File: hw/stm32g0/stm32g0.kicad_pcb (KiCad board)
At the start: 4 copper layers, 80 x 40 mm, 74 parts, among them J101 Barrel_Jack_Switch, J102 Screw_Terminal_01x03, J201 Conn_01x06, J202 Conn_01x04, J203 Conn_01x05, Q101 BC817, SW401 SW_Push, SW402 SW_Push, SW403 SW_Push, SW404 SW_Push, SW405 SW_Push, SW406 SW_Push, U201 STM32G030K8Tx, U202 74AHCT125, U203 CAT24C256, U301 VS1838B, U401 4050, U501 AMS1117-3.3

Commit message: chore(hw): improve layout
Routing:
- net GND: track 144.7 -> 155.6 mm, vias 51 -> 50
- net +5V: track 145.7 -> 141.7 mm
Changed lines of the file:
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@@
 	)
 	(segment
-		(start 192.151 89.615)
+		(start 184.277 90.424)
+		(end 191.897 90.424)
+		(width 1.5)
+		(layer "In2.Cu")
+		(net 1)
+	)
+	(segment
+		(start 192.706 89.615)
 		(end 194.183 89.615)
 		(width 1.5)
-		(layer "In1.Cu")
+		(layer "In2.Cu")
 		(net 1)
 	)
 	(segment
 		(start 182.118 91.069)
-		(end 182.763 90.424)
+		(end 183.632 91.069)
 		(width 1.5)
-		(layer "In1.Cu")
-		(net 1)
-	)
-	(segment
-		(start 191.342 90.424)
-		(end 192.151 89.615)
+		(layer "In2.Cu")
+		(net 1)
+	)
+	(segment
+		(start 191.897 90.424)
+		(end 192.706 89.615)
 		(width 1.5)
-		(layer "In1.Cu")
-		(net 1)
-	)
-	(segment
-		(start 182.763 90.424)
-		(end 191.342 90.424)
+		(layer "In2.Cu")
+		(net 1)
+	)
+	(segment
+		(start 183.632 91.069)
+		(end 184.277 90.424)
 		(width 1.5)
-		(layer "In1.Cu")
+		(layer "In2.Cu")
+		(net 1)
+	)
+	(segment
+		(start 171.577 95.123)
+		(end 175.26 98.806)
+		(width 0.5)
+		(layer "B.Cu")
 		(net 1)
 	)
@@
 	)
 	(segment
-		(start 182.118 92.869)
-		(end 173.069 92.869)
-		(width 0.5)
-		(layer "B.Cu")
-		(net 1)
-	)
-	(segment
 		(start 142.113 111.379)
 		(end 140.716 111.379)
@@
 	)
 	(segment
+		(start 175.26 98.806)
+		(end 175.26 100.33)
+		(width 0.5)
+		(layer "B.Cu")
+		(net 1)
+	)
+	(segment
 		(start 162.052 102.23501)
 		(end 169.672 102.23501)
@@
 		(end 161.544 109.728)
 		(width 0.3)
-		(layer "B.Cu")
-		(net 1)
-	)
-	(segment
-		(start 175.26 100.33)
-		(end 175.26 98.425)
-		(width 0.5)
 		(layer "B.Cu")
 		(net 1)
@@
 	)
 	(segment
-		(start 180.499 94.488)
-		(end 182.118 92.869)
-		(width 0.5)
-		(layer "B.Cu")
-		(net 1)
-	)
-	(segment
-		(start 175.26 98.425)
-		(end 179.197 94.488)
-		(width 0.5)
-		(layer "B.Cu")
-		(net 1)
-	)
-	(segment
 		(start 175.26 100.33)
 		(end 175.26 104.77499)
@@
 	)
 	(segment
+		(start 173.831 92.869)
+		(end 171.577 95.123)
+		(width 0.7)
+		(layer "B.Cu")
+		(net 1)
+	)
+	(segment
 		(start 171.57701 100.33)
 		(end 175.26 100.33)
@@
 	)
 	(segment
+		(start 182.118 92.869)
+		(end 173.831 92.869)
+		(width 0.7)
+		(layer "B.Cu")
+		(net 1)
+	)
+	(segment
 		(start 156.464 100.457)
 		(end 160.27399 100.457)
@@
 	)
 	(segment
-		(start 173.069 92.869)
-		(end 171.577 94.361)
-		(width 0.5)
-		(layer "B.Cu")
-		(net 1)
-	)
-	(segment
-		(start 179.197 94.488)
-		(end 180.499 94.488)
-		(width 0.5)
-		(layer "B.Cu")
-		(net 1)
-	)
-	(segment
 		(start 143.764 109.728)
 		(end 142.113 111.379)
@@
 		(layer "F.Cu")
 		(net 2)
+	)
+	(segment
+		(start 185.674 103.886)
+		(end 185.674 105.283)
+		(width 0.3)
+		(layer "F.Cu")
+		(net 3)
 	)
 	(segment
@@
 	)
 	(segment
-		(start 185.547 103.759)
-		(end 185.674 103.886)
-		(width 0.3)
-		(layer "F.Cu")
-		(net 3)
-	)
-	(segment
 		(start 153.035 101.854)
 		(end 152.908 101.727)
@@
 		(end 160.4225 90.0645)
 		(width 0.4)
-		(layer "F.Cu")
-		(net 3)
-	)
-	(segment
-		(start 185.674 103.886)
-		(end 185.674 106.172)
-		(width 0.3)
 		(layer "F.Cu")
 		(net 3)
@@
 	)
 	(segment
+		(start 185.547 103.759)
+		(end 185.674 103.886)
+		(width 0.3)
+		(layer "F.Cu")
+		(net 3)
+	)
+	(segment
 		(start 179.4256 79.0956)
 		(end 179.832 79.502)
@@
 	)
 	(segment
+		(start 185.674 105.283)
+		(end 185.547 105.41)
+		(width 0.3)
+		(layer "F.Cu")
+		(net 3)
+	)
+	(segment
 		(start 181.864 78.486)
 		(end 182.118 78.232)
@@
 	)
 	(via
-		(at 176.784 94.361)
-		(size 0.8)
-		(drill 0.4)
-		(layers "F.Cu" "B.Cu")
-		(free yes)
-		(net 3)
-	)
-	(via
 		(at 190.119 104.14)
 		(size 0.8)
@@
 		(layers "F.Cu" "B.Cu")
 		(free yes)
+		(net 3)
+	)
+	(segment
+		(start 188.976 104.14)
+		(end 190.119 104.14)
+		(width 0.3)
+		(layer "B.Cu")
+		(net 3)
+	)
+	(segment
+		(start 155.406 96.944337)
+		(end 155.406 90.974)
+		(width 0.3)
+		(layer "B.Cu")
+		(net 3)
+	)
+	(segment
+		(start 147.447 104.648)
+		(end 147.702337 104.648)
+		(width 0.3)
+		(layer "B.Cu")
+		(net 3)
+	)
+	(segment
+		(start 160.528 82.804)
+		(end 165.227 82.804)
+		(width 0.3)
+		(layer "B.Cu")
+		(net 3)
+	)
+	(segment
+		(start 186.055 100.457)
+		(end 186.055 101.219)
+		(width 0.3)
+		(layer "B.Cu")
+		(net 3)
+	)
+	(segment
+		(start 159.766 83.058)
+		(end 160.274 83.058)
+		(width 0.3)
+		(layer "B.Cu")
+		(net 3)
+	)
+	(segment
+		(start 186.444 100.068)
+		(end 186.055 100.457)
+		(width 0.3)
+		(layer "B.Cu")
+		(net 3)
+	)
+	(segment
+		(start 186.055 101.219)
+		(end 188.976 104.14)
+		(width 0.3)
+		(layer "B.Cu")
+		(net 3)
+	)
+	(segment
+		(start 184.794214 81.907)
+		(end 186.444 83.556786)
+		(width 0.3)
+		(layer "B.Cu")
+		(net 3)
+	)
+	(segment
+		(start 160.274 83.058)
+		(end 160.528 82.804)
+		(width 0.3)
+		(layer "B.Cu")
 		(net 3)
 	)
@@
 	)
 	(segment
-		(start 155.406 96.944337)
-		(end 155.406 90.974)
-		(width 0.3)
-		(layer "B.Cu")
-		(net 3)
-	)
-	(segment
-		(start 184.794214 81.907)
-		(end 186.444 83.556786)
-		(width 0.3)
-		(layer "B.Cu")
-		(net 3)
-	)
-	(segment
-		(start 147.447 104.648)
-		(end 147.702337 104.648)
+		(start 147.702337 104.648)
+		(end 155.406 96.944337)
+		(width 0.3)
+		(layer "B.Cu")
+		(net 3)
+	)
+	(segment
+		(start 155.406 90.974)
+		(end 155.829 90.551)
 		(width 0.3)
 		(layer "B.Cu")
@@
 	)
 	(segment
+		(start 147.066 105.029)
+		(end 147.447 104.648)
+		(width 0.3)
+		(layer "B.Cu")
+		(net 3)
+	)
+	(segment
 		(start 165.227 82.804)
 		(end 166.124 81.907)
-		(width 0.3)
-		(layer "B.Cu")
-		(net 3)
-	)
-	(segment
-		(start 186.444 100.068)
-		(end 186.055 100.457)
-		(width 0.3)
-		(layer "B.Cu")
-		(net 3)
-	)
-	(segment
-		(start 147.702337 104.648)
-		(end 155.406 96.944337)
-		(width 0.3)
-		(layer "B.Cu")
-		(net 3)
-	)
-	(segment
-		(start 155.406 90.974)
-		(end 155.829 90.551)
-		(width 0.3)
-		(layer "B.Cu")
-		(net 3)
-	)
-	(segment
-		(start 147.066 105.029)
-		(end 147.447 104.648)
 		(width 0.3)
 		(layer "B.Cu")
@@
 	)
 	(segment
+		(start 175.895 86.487)
+		(end 161.163 86.487)
+		(width 0.3)
+		(layer "B.Cu")
+		(net 14)
+	)
+	(segment
+		(start 161.163 86.487)
+		(end 160.274 85.598)
+		(width 0.3)
+		(layer "B.Cu")
+		(net 14)
+	)
+	(segment
 		(start 150.741 84.701)
 		(end 149.606 83.566)
@@
 	)
 	(segment
-		(start 174.879 86.106)
-		(end 160.782 86.106)
-		(width 0.3)
-		(layer "B.Cu")
-		(net 14)
-	)
-	(segment
-		(start 160.782 86.106)
-		(end 160.274 85.598)
-		(width 0.3)
-		(layer "B.Cu")
-		(net 14)
-	)
-	(segment
-		(start 175.895 86.487)
-		(end 175.26 86.487)
-		(width 0.3)
-		(layer "B.Cu")
-		(net 14)
-	)
-	(segment
 		(start 148.463 83.566)
 		(end 147.193 82.296)
@@
 		(width 0.3)
 		(layer "B.Cu")
-		(net 14)
-	)
-	(segment
-		(start 175.26 86.487)
-		(end 174.879 86.106)
-		(width 0.3)
-		(layer "B.Cu")

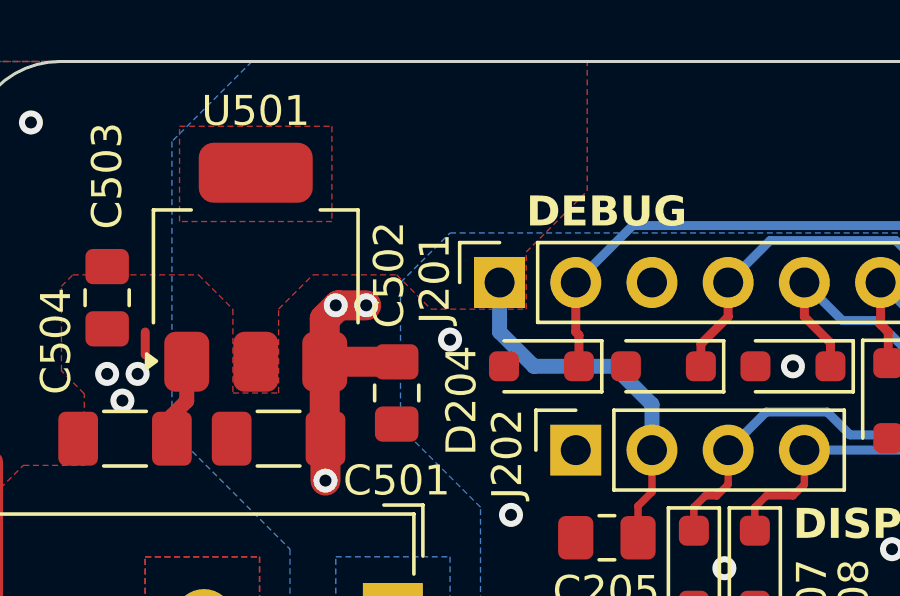
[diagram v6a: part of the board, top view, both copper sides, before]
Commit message: chore(hw): change debug port to pin header
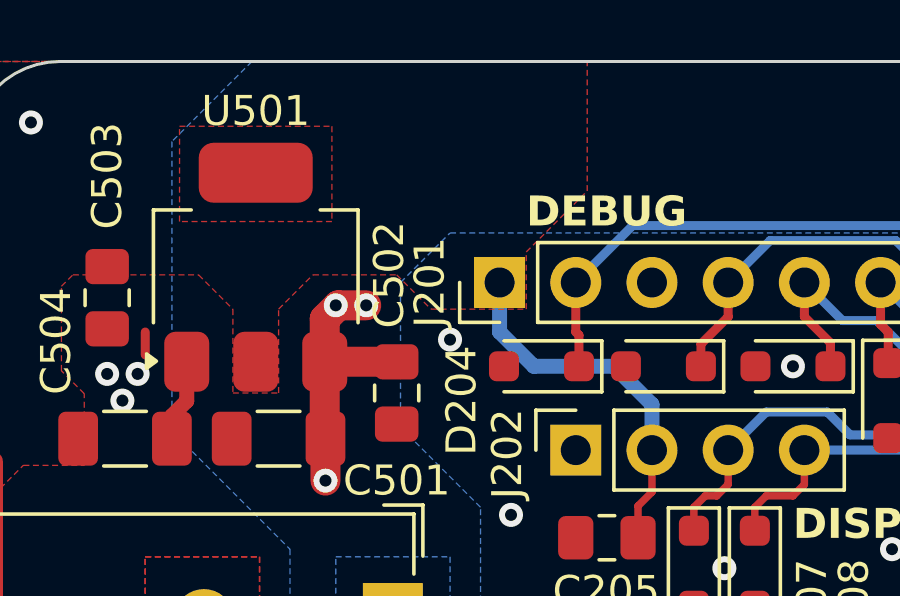
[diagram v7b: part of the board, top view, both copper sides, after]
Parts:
- J201: footprint Connector_PinSocket_2.54mm:PinSocket_1x06_P2.54mm_Vertical -> Connector_PinHeader_2.54mm:PinHeader_1x06_P2.54mm_Vertical
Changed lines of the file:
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@@
 		)
 	)
-	(footprint "Connector_PinSocket_2.54mm:PinSocket_1x06_P2.54mm_Vertical"
+	(footprint "Connector_PinHeader_2.54mm:PinHeader_1x06_P2.54mm_Vertical"
 		(layer "F.Cu")
 		(at 137.033 82.296 90)
-		(descr "Through hole straight socket strip, 1x06, 2.54mm pitch, single row (from Kicad 4.0.7), script generated")
-		(tags "Through hole socket strip THT 1x06 2.54mm single row")
+		(descr "Through hole straight pin header, 1x06, 2.54mm pitch, single row")
+		(tags "Through hole pin header THT 1x06 2.54mm single row")
 		(property "Reference" "J201"
-			(at 0.127 -2.159 -90)
+			(at 0 -2.33 90)
 			(layer "F.SilkS")
 			(effects
@@
 		)
 		(property "Value" "Conn_01x06"
-			(at 2.54 -2.159 -90)
+			(at 0 15.03 90)
 			(layer "F.Fab")
 			(effects
@@
 			)
 		)
-		(property "Footprint" "Connector_PinSocket_2.54mm:PinSocket_1x06_P2.54mm_Vertical"
+		(property "Footprint" "Connector_PinHeader_2.54mm:PinHeader_1x06_P2.54mm_Vertical"
 			(at 0 0 90)
 			(unlocked yes)
@@
 		(attr through_hole dnp)
 		(fp_line
-			(start 1.33 -1.33)
-			(end 1.33 0)
-			(stroke
-				(width 0.12)
-				(type solid)
-			)
-			(layer "F.SilkS")
-		)
-		(fp_line
-			(start 0 -1.33)
-			(end 1.33 -1.33)
+			(start -1.33 -1.33)
+			(end 0 -1.33)
+			(stroke
+				(width 0.12)
+				(type solid)
+			)
+			(layer "F.SilkS")
+		)
+		(fp_line
+			(start -1.33 0)
+			(end -1.33 -1.33)
 			(stroke
 				(width 0.12)
@@
 		)
 		(fp_line
-			(start 1.75 -1.8)
-			(end 1.75 14.45)
+			(start 1.8 -1.8)
+			(end -1.8 -1.8)
 			(stroke
 				(width 0.05)
@@
 		(fp_line
 			(start -1.8 -1.8)
-			(end 1.75 -1.8)
-			(stroke
-				(width 0.05)
-				(type solid)
-			)
-			(layer "F.CrtYd")
-		)
-		(fp_line
-			(start 1.75 14.45)
-			(end -1.8 14.45)
-			(stroke
-				(width 0.05)
-				(type solid)
-			)
-			(layer "F.CrtYd")
-		)
-		(fp_line
-			(start -1.8 14.45)
-			(end -1.8 -1.8)
-			(stroke
-				(width 0.05)
-				(type solid)
-			)
-			(layer "F.CrtYd")
-		)
-		(fp_line
-			(start 0.635 -1.27)
-			(end 1.27 -0.635)
-			(stroke
-				(width 0.1)
-				(type solid)
-			)
-			(layer "F.Fab")
-		)
-		(fp_line
-			(start -1.27 -1.27)
-			(end 0.635 -1.27)
-			(stroke
-				(width 0.1)
-				(type solid)
-			)
-			(layer "F.Fab")
-		)
-		(fp_line
-			(start 1.27 -0.635)
+			(end -1.8 14.5)
+			(stroke
+				(width 0.05)
+				(type solid)
+			)
+			(layer "F.CrtYd")
+		)
+		(fp_line
+			(start 1.8 14.5)
+			(end 1.8 -1.8)
+			(stroke
+				(width 0.05)
+				(type solid)
+			)
+			(layer "F.CrtYd")
+		)
+		(fp_line
+			(start -1.8 14.5)
+			(end 1.8 14.5)
+			(stroke
+				(width 0.05)
+				(type solid)
+			)
+			(layer "F.CrtYd")
+		)
+		(fp_line
+			(start 1.27 -1.27)
 			(end 1.27 13.97)
+			(stroke
+				(width 0.1)
+				(type solid)
+			)
+			(layer "F.Fab")
+		)
+		(fp_line
+			(start -0.635 -1.27)
+			(end 1.27 -1.27)
+			(stroke
+				(width 0.1)
+				(type solid)
+			)
+			(layer "F.Fab")
+		)
+		(fp_line
+			(start -1.27 -0.635)
+			(end -0.635 -1.27)
 			(stroke
 				(width 0.1)
@@
 		(fp_line
 			(start -1.27 13.97)
-			(end -1.27 -1.27)
+			(end -1.27 -0.635)
 			(stroke
 				(width 0.1)
@@
 		)
 		(fp_text user "${REFERENCE}"
-			(at 0 6.35 0)
+			(at 0 6.35 180)
 			(layer "F.Fab")
 			(effects
@@
 			(pintype "passive")
 		)
-		(model "${KICAD8_3DMODEL_DIR}/Connector_PinSocket_2.54mm.3dshapes/PinSocket_1x06_P2.54mm_Vertical.wrl"
+		(model "${KICAD8_3DMODEL_DIR}/Connector_PinHeader_2.54mm.3dshapes/PinHeader_1x06_P2.54mm_Vertical.wrl"
 			(offset
 				(xyz 0 0 0)

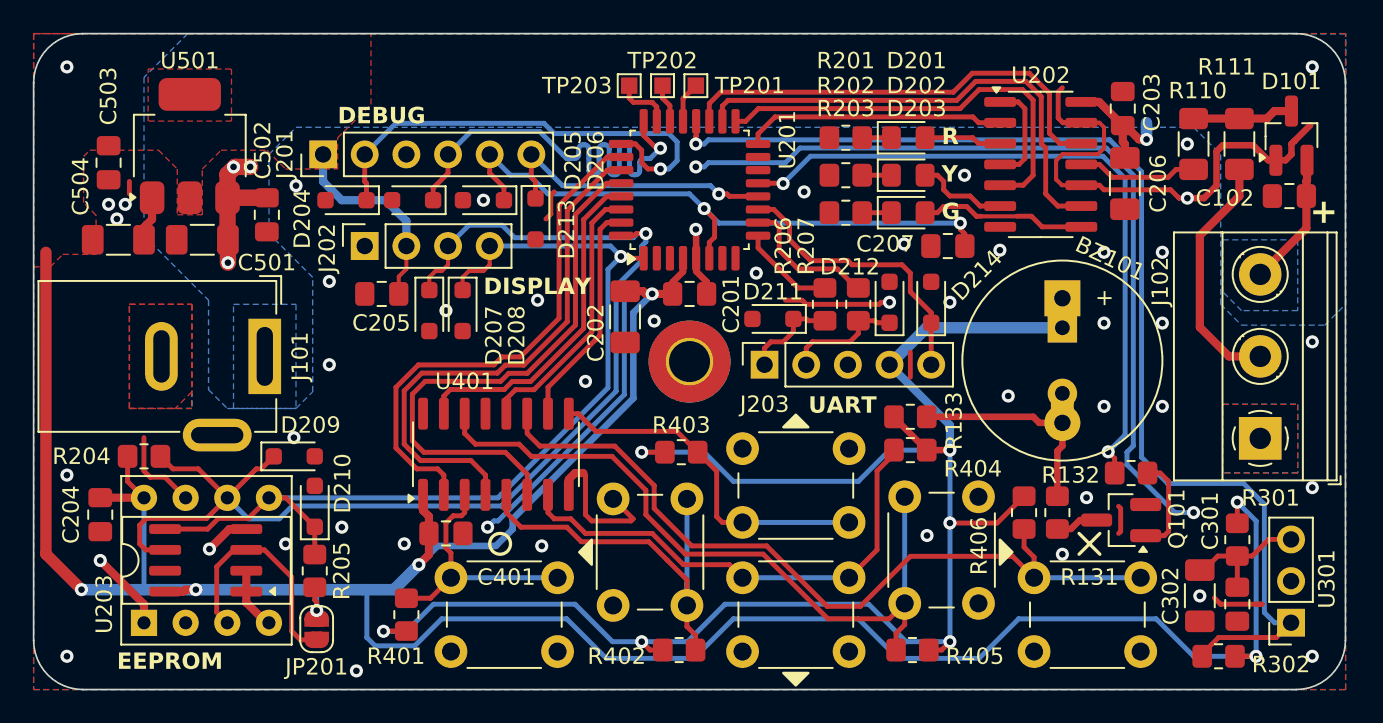
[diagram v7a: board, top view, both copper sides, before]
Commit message: chore(hw): improve i2c layout
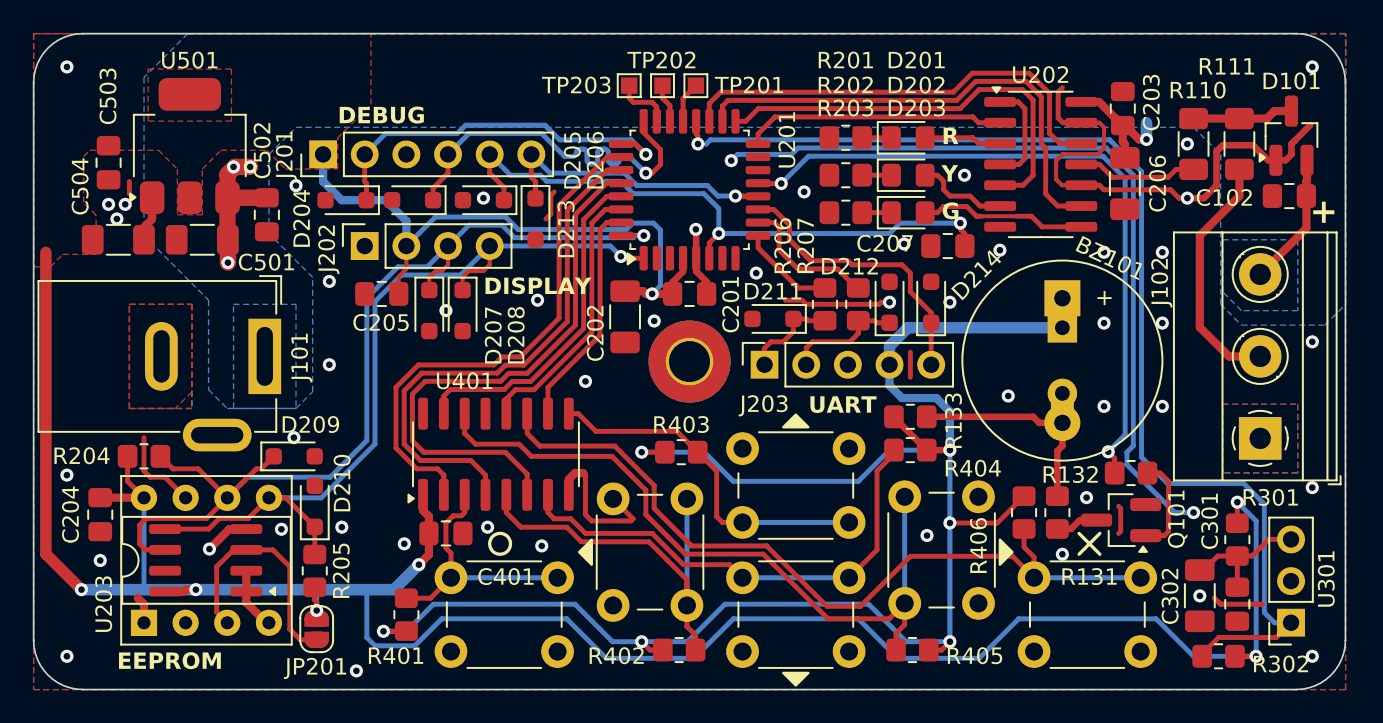
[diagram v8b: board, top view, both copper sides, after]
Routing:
- net GND: track 155.6 -> 131.8 mm
- net /CPU/I2C_SCL: track 73.7 -> 60.4 mm
- net /CPU/I2C_SDA: track 58.5 -> 51.6 mm
- net /CPU/SWCLK: track 29.0 -> 23.2 mm
- net /CPU/SWDIO: track 29.2 -> 23.5 mm
- net +3.3V: track 181.1 -> 177.6 mm
- net +5V: track 141.7 -> 143.6 mm
